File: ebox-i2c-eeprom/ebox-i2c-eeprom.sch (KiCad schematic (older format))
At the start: 11 parts, among them J1 xconch_pinheader_2x40, J2 xconch_pinsocket_2x40, U1 AT24CS64-SSHM

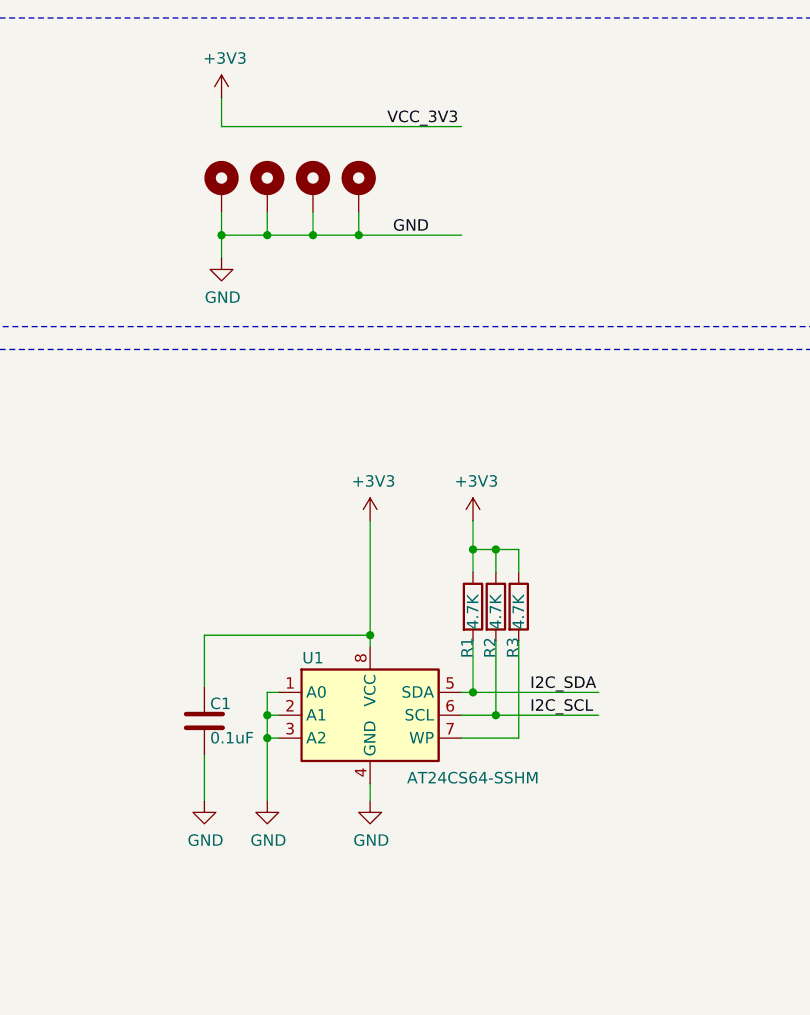
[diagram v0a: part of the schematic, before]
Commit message: [ebox]add ebox-i2c eeprom
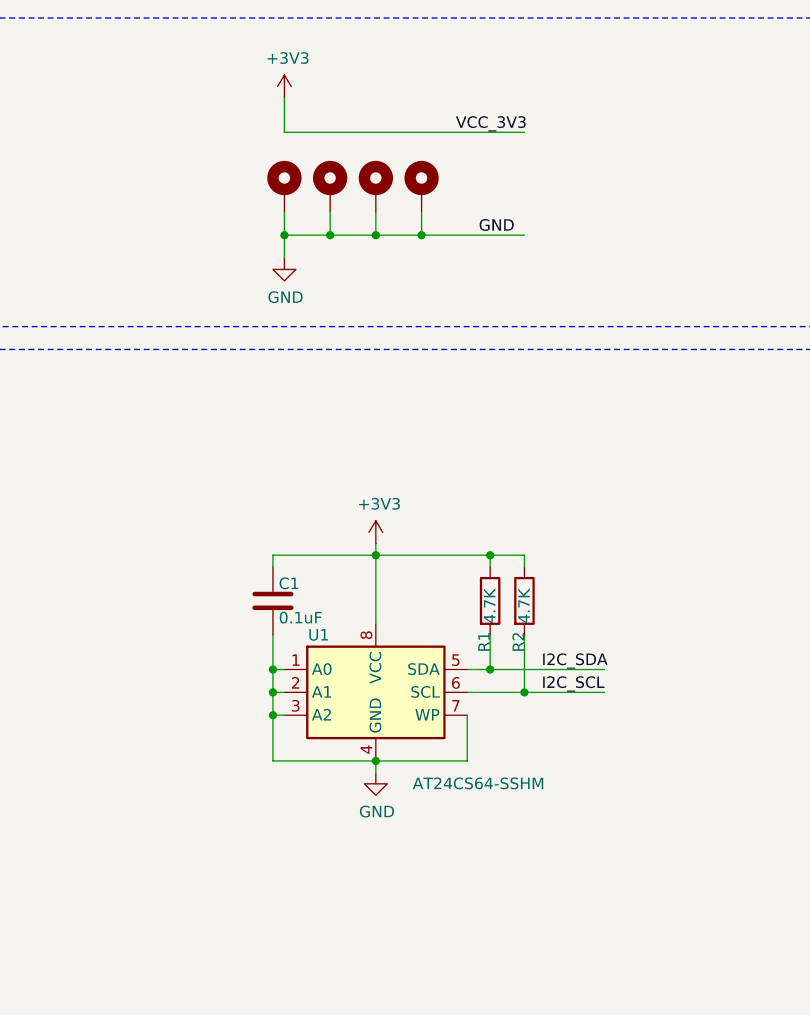
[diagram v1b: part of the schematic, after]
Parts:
- removed R3: 4.7K, Resistor_SMD:R_0402_1005Metric, symbol Device:R
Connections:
- wire segments 157 -> 156
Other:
- moved on the sheet: C1, R1, R2, U1

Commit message: working on ebox i2c eeprom
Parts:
- U1: value AT24CS64-SSHM -> AT24C64
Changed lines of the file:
@@
 L power:GND #PWR06
 U 1 1 5AC2A3B5
-P 8450 4900
-F 0 "#PWR06" H 8450 4650 50  0001 C CNN
-F 1 "GND" H 8455 4727 50  0000 C CNN
-F 2 "" H 8450 4900 50  0001 C CNN
-F 3 "" H 8450 4900 50  0001 C CNN
-	1    8450 4900
+P 8000 4900
+F 0 "#PWR06" H 8000 4650 50  0001 C CNN
+F 1 "GND" H 8005 4727 50  0000 C CNN
+F 2 "" H 8000 4900 50  0001 C CNN
+F 3 "" H 8000 4900 50  0001 C CNN
+	1    8000 4900
 	1    0    0    -1
 $EndComp
@@
 U 1 1 5ABE2B5D
 P 8450 4550
-F 0 "U1" H 8200 4800 50  0000 C CNN
-F 1 "AT24CS64-SSHM" H 8900 4150 50  0000 C CNN
+F 0 "U1" H 8600 4800 50  0000 C CNN
+F 1 "AT24C64" H 8450 4150 50  0000 C CNN
 F 2 "Package_SO:SOIC-8_3.9x4.9mm_P1.27mm" H 8450 4550 50  0001 C CNN
 F 3 "http://ww1.microchip.com/downloads/en/DeviceDoc/Atmel-8870-SEEPROM-AT24CS64-Datasheet.pdf" H 8450 4550 50  0001 C CNN
@@
 	8850 4850 8450 4850
 Connection ~ 8450 4850
-Wire Wire Line
-	8450 4900 8450 4850
 Wire Wire Line
 	8050 4550 8000 4550
@@
 Wire Wire Line
 	8000 3950 8000 4000
+Wire Wire Line
+	8000 4900 8000 4850
+Connection ~ 8000 4850
 $EndSCHEMATC
